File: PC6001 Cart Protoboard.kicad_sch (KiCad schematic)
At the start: 20 parts, among them J1 PC-6001 edge connector, SW1 PicoReset, SW2 EspReset, SW3 Button A, U2 ESP32-DevKitC, U3 74LS32, U4 microSD-Breakout, U5 74LS08, U6 SN74LVC245AN, U7 SN74LVC245AN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

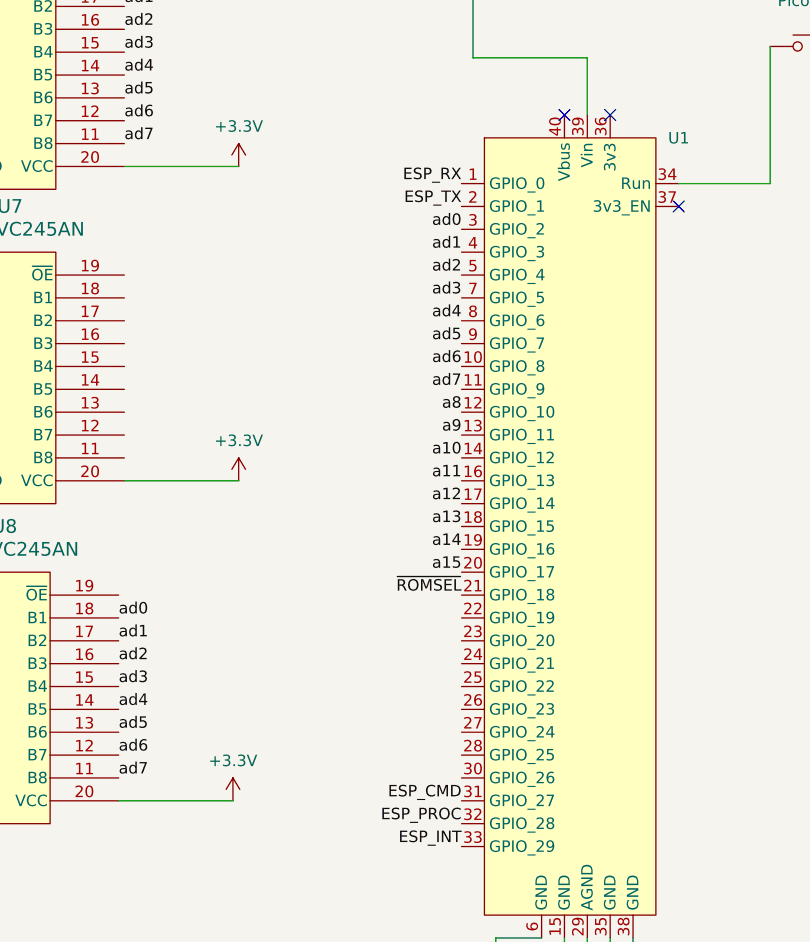
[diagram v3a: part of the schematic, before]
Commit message: Wire in ramsel and wr so now we can be sram
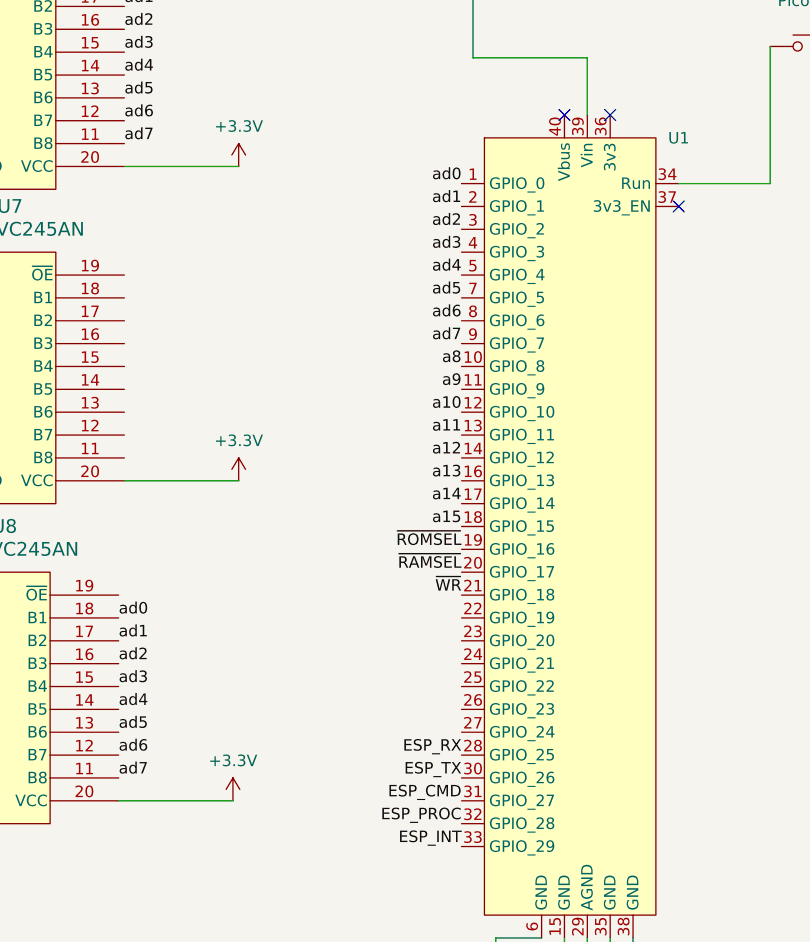
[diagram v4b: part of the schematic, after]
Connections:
- net ESP_RX: now also U1.28 (GPIO_25); no longer U1.1 (GPIO_0)
- net ESP_TX: now also U1.30 (GPIO_26); no longer U1.2 (GPIO_1)
- net a10: now also U1.12 (GPIO_10); no longer U1.14 (GPIO_12)
- net a11: now also U1.13 (GPIO_11); no longer U1.16 (GPIO_13)
- net a12: now also U1.14 (GPIO_12); no longer U1.17 (GPIO_14)
- net a13: now also U1.16 (GPIO_13); no longer U1.18 (GPIO_15)
- net a14: now also U1.17 (GPIO_14); no longer U1.19 (GPIO_16)
- net a15: now also U1.18 (GPIO_15); no longer U1.20 (GPIO_17)
- net a8: now also U1.10 (GPIO_8); no longer U1.12 (GPIO_10)
- net a9: now also U1.11 (GPIO_9); no longer U1.13 (GPIO_11)
- net ad0: now also U1.1 (GPIO_0); no longer U1.3 (GPIO_2)
- net ad1: now also U1.2 (GPIO_1); no longer U1.4 (GPIO_3)
- net ad2: now also U1.3 (GPIO_2); no longer U1.5 (GPIO_4)
- net ad3: now also U1.4 (GPIO_3); no longer U1.7 (GPIO_5)
- net ad4: now also U1.5 (GPIO_4); no longer U1.8 (GPIO_6)
- net ad5: now also U1.7 (GPIO_5); no longer U1.9 (GPIO_7)
- net ad6: now also U1.8 (GPIO_6); no longer U1.10 (GPIO_8)
- net ad7: now also U1.9 (GPIO_7); no longer U1.11 (GPIO_9)
- net ~{RAMSEL}: now also U1.20 (GPIO_17)
- net ~{ROMSEL}: now also U1.19 (GPIO_16); no longer U1.21 (GPIO_18)
- net ~{WR}: now also U1.21 (GPIO_18)
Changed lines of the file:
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@@
 	)
 	(label "a12"
-		(at 172.085 96.52 180)
+		(at 172.085 91.44 180)
 		(fields_autoplaced yes)
 		(effects
@@
 	)
 	(label "ad3"
-		(at 172.085 73.66 180)
+		(at 172.085 68.58 180)
 		(fields_autoplaced yes)
 		(effects
@@
 	)
 	(label "a11"
-		(at 172.085 93.98 180)
+		(at 172.085 88.9 180)
 		(fields_autoplaced yes)
 		(effects
@@
 	)
 	(label "a10"
-		(at 172.085 91.44 180)
+		(at 172.085 86.36 180)
 		(fields_autoplaced yes)
 		(effects
@@
 	)
 	(label "~{ROMSEL}"
-		(at 172.085 106.68 180)
+		(at 172.085 101.6 180)
 		(fields_autoplaced yes)
 		(effects
@@
 	)
 	(label "a15"
-		(at 172.085 104.14 180)
+		(at 172.085 99.06 180)
 		(fields_autoplaced yes)
 		(effects
@@
 	)
 	(label "ESP_RX"
-		(at 172.085 60.96 180)
+		(at 172.085 124.46 180)
 		(fields_autoplaced yes)
 		(effects
@@
 	)
 	(label "ESP_TX"
-		(at 172.085 63.5 180)
+		(at 172.085 127 180)
 		(fields_autoplaced yes)
 		(effects
@@
 	)
 	(label "ad4"
-		(at 172.085 76.2 180)
+		(at 172.085 71.12 180)
 		(fields_autoplaced yes)
 		(effects
@@
 	)
 	(label "a13"
-		(at 172.085 99.06 180)
+		(at 172.085 93.98 180)
 		(fields_autoplaced yes)
 		(effects
@@
 	)
 	(label "a14"
-		(at 172.085 101.6 180)
+		(at 172.085 96.52 180)
 		(fields_autoplaced yes)
 		(effects
@@
 	)
 	(label "ad5"
-		(at 172.085 78.74 180)
+		(at 172.085 73.66 180)
 		(fields_autoplaced yes)
 		(effects
@@
 		)
 	)
+	(label "~{RAMSEL}"
+		(at 172.085 104.14 180)
+		(fields_autoplaced yes)
+		(effects
+			(font
+				(size 1.27 1.27)
+			)
+			(justify right bottom)
+		)
+	)
 	(label "ad0"
-		(at 172.085 66.04 180)
+		(at 172.085 60.96 180)
 		(fields_autoplaced yes)
 		(effects
@@
 		)
 	)
+	(label "~{WR}"
+		(at 172.085 106.68 180)
+		(fields_autoplaced yes)
+		(effects
+			(font
+				(size 1.27 1.27)
+			)
+			(justify right bottom)
+		)
+	)
 	(label "a10"
 		(at 64.135 101.6 0)
@@
 	)
 	(label "ad7"
-		(at 172.085 83.82 180)
+		(at 172.085 78.74 180)
 		(fields_autoplaced yes)
 		(effects
@@
 	)
 	(label "ad1"
-		(at 172.085 68.58 180)
+		(at 172.085 63.5 180)
 		(fields_autoplaced yes)
 		(effects
@@
 	)
 	(label "a9"
-		(at 172.085 88.9 180)
+		(at 172.085 83.82 180)
 		(fields_autoplaced yes)
 		(effects
@@
 	)
 	(label "ad2"
-		(at 172.085 71.12 180)
+		(at 172.085 66.04 180)
 		(fields_autoplaced yes)
 		(effects
@@
 	)
 	(label "ad6"
-		(at 172.085 81.28 180)
+		(at 172.085 76.2 180)
 		(fields_autoplaced yes)
 		(effects
@@
 	)
 	(label "a8"
-		(at 172.085 86.36 180)
-		(fields_autoplaced yes)
-		(effects
+		(at 172.085 81.28 180)
+		(fields_autoplaced yes)
+		(effects

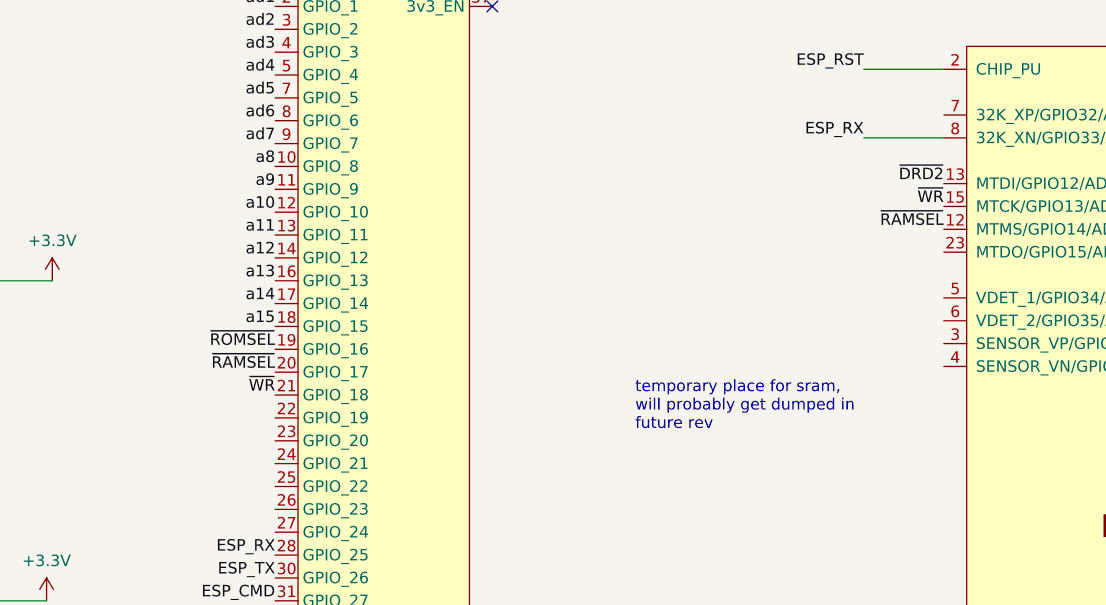
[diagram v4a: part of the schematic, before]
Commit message: Add IORQ and CS3
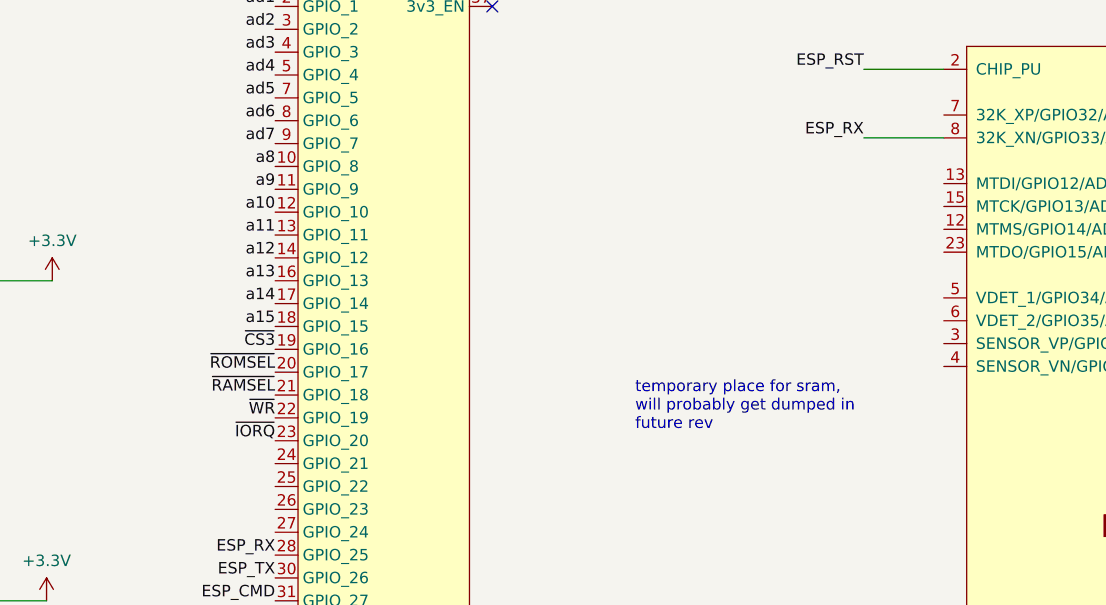
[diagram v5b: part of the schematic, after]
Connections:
- net ~{CS3}: now also U1.19 (GPIO_16)
- net ~{DRD2}: no longer U2.13 (MTDI/GPIO12/ADC2_CH5)
- net ~{RAMSEL}: now also U1.21 (GPIO_18); no longer U1.20 (GPIO_17), U2.12 (MTMS/GPIO14/ADC2_CH6)
- net ~{ROMSEL}: now also U1.20 (GPIO_17); no longer U1.19 (GPIO_16)
- net ~{WR}: now also U1.22 (GPIO_19); no longer U1.21 (GPIO_18), U2.15 (MTCK/GPIO13/ADC2_CH4)
- net ~{IORQ}: now reaches U1.23 (GPIO_20)
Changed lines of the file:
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@@
 	)
 	(label "~{ROMSEL}"
-		(at 172.085 101.6 180)
+		(at 172.085 104.14 180)
 		(fields_autoplaced yes)
 		(effects
@@
 		)
 	)
-	(label "~{DRD2}"
-		(at 246.38 83.185 180)
-		(fields_autoplaced yes)
-		(effects
-			(font
-				(size 1.27 1.27)
-			)
-			(justify right bottom)
-		)
-	)
 	(label "ad2"
 		(at 134.62 43.815 0)
@@
 		)
 	)
-	(label "~{WR}"
-		(at 246.38 85.725 180)
-		(fields_autoplaced yes)
-		(effects
-			(font
-				(size 1.27 1.27)
-			)
-			(justify right bottom)
-		)
-	)
-	(label "~{RAMSEL}"
-		(at 246.38 88.265 180)
-		(fields_autoplaced yes)
-		(effects
-			(font
-				(size 1.27 1.27)
-			)
-			(justify right bottom)
-		)
-	)
 	(label "d3"
 		(at 108.585 116.84 180)
@@
 	)
 	(label "~{RAMSEL}"
-		(at 172.085 104.14 180)
+		(at 172.085 106.68 180)
 		(fields_autoplaced yes)
 		(effects
@@
 		)
 	)
+	(label "~{CS3}"
+		(at 172.085 101.6 180)
+		(fields_autoplaced yes)
+		(effects
+			(font
+				(size 1.27 1.27)
+			)
+			(justify right bottom)
+		)
+	)
 	(label "d5"
 		(at 108.585 121.92 180)
@@
 	)
 	(label "~{WR}"
-		(at 172.085 106.68 180)
+		(at 172.085 109.22 180)
 		(fields_autoplaced yes)
 		(effects
@@
 		(fields_autoplaced yes)
 		(effects
+			(font
+				(size 1.27 1.27)
+			)
+			(justify right bottom)
+		)
+	)
+	(label "~{IORQ}"
+		(at 172.085 111.76 180)
+		(fields_autoplaced yes)
+		(effects

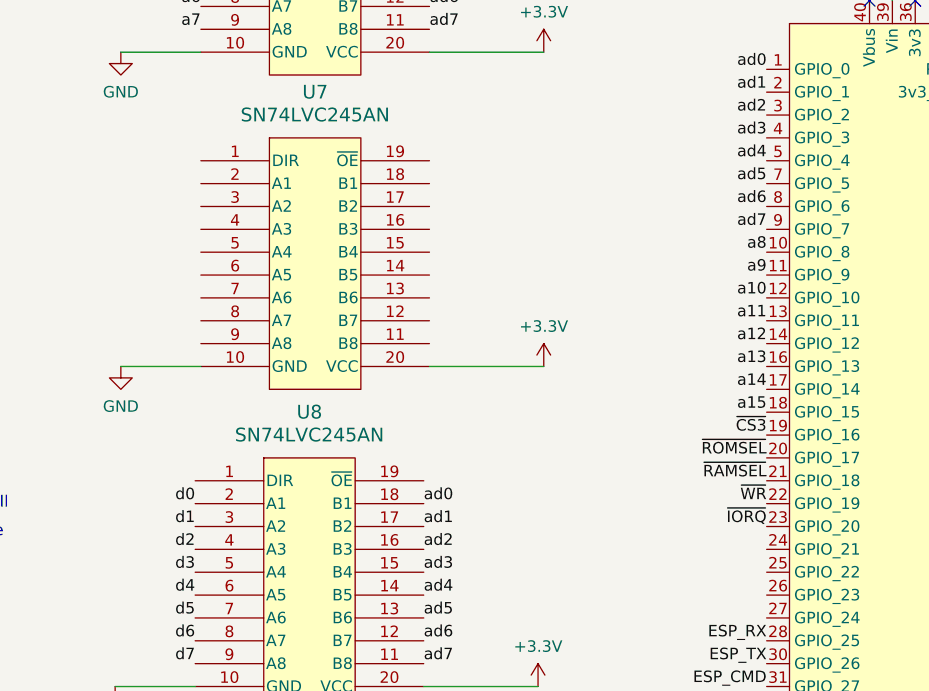
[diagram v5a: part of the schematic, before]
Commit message: Move high address lines to 245
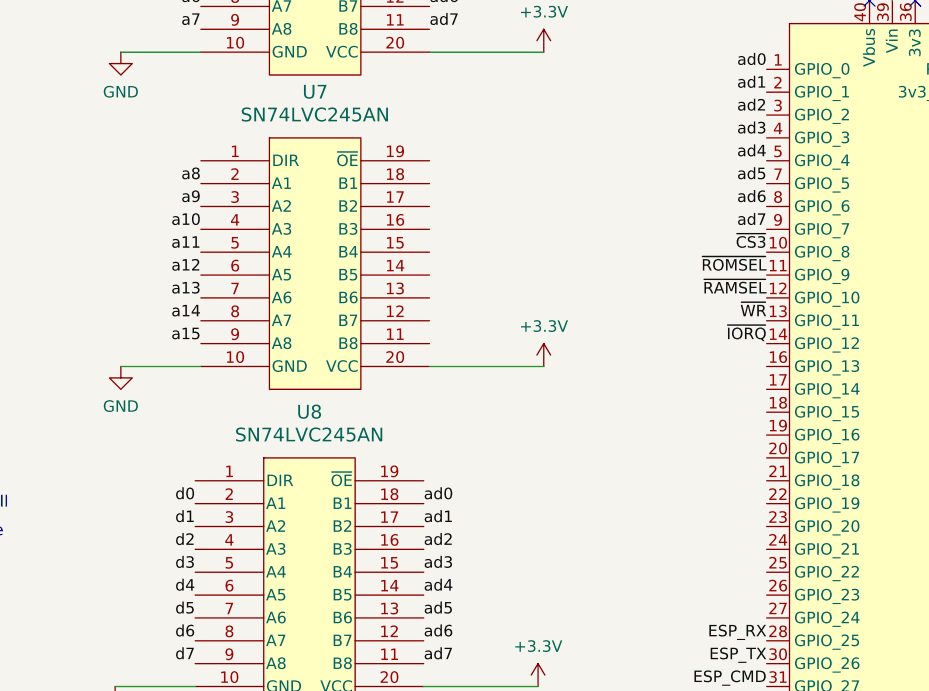
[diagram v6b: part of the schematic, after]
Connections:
- net a10: now also U7.4 (A3); no longer U1.12 (GPIO_10)
- net a11: now also U7.5 (A4); no longer U1.13 (GPIO_11)
- net a12: now also U7.6 (A5); no longer U1.14 (GPIO_12)
- net a13: now also U7.7 (A6); no longer U1.16 (GPIO_13)
- net a14: now also U7.8 (A7); no longer U1.17 (GPIO_14)
- net a15: now also U7.9 (A8); no longer U1.18 (GPIO_15)
- net a8: now also U7.2 (A1); no longer U1.10 (GPIO_8)
- net a9: now also U7.3 (A2); no longer U1.11 (GPIO_9)
- net ~{CS3}: now also U1.10 (GPIO_8); no longer U1.19 (GPIO_16)
- net ~{IORQ}: now also U1.14 (GPIO_12); no longer U1.23 (GPIO_20)
- net ~{RAMSEL}: now also U1.12 (GPIO_10); no longer U1.21 (GPIO_18)
- net ~{ROMSEL}: now also U1.11 (GPIO_9); no longer U1.20 (GPIO_17)
- net ~{WR}: now also U1.13 (GPIO_11); no longer U1.22 (GPIO_19)
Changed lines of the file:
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@@
 	)
 	(label "a12"
-		(at 172.085 91.44 180)
+		(at 109.22 83.82 180)
 		(fields_autoplaced yes)
 		(effects
@@
 	)
 	(label "a11"
-		(at 172.085 88.9 180)
+		(at 109.22 81.28 180)
 		(fields_autoplaced yes)
 		(effects
@@
 	)
 	(label "a10"
-		(at 172.085 86.36 180)
+		(at 109.22 78.74 180)
 		(fields_autoplaced yes)
 		(effects
@@
 	)
 	(label "~{ROMSEL}"
-		(at 172.085 104.14 180)
+		(at 172.085 83.82 180)
 		(fields_autoplaced yes)
 		(effects
@@
 	)
 	(label "a15"
-		(at 172.085 99.06 180)
+		(at 109.22 91.44 180)
 		(fields_autoplaced yes)
 		(effects
@@
 	)
 	(label "a13"
-		(at 172.085 93.98 180)
+		(at 109.22 86.36 180)
 		(fields_autoplaced yes)
 		(effects
@@
 	)
 	(label "a14"
-		(at 172.085 96.52 180)
+		(at 109.22 88.9 180)
 		(fields_autoplaced yes)
 		(effects
@@
 	)
 	(label "~{RAMSEL}"
-		(at 172.085 106.68 180)
+		(at 172.085 86.36 180)
 		(fields_autoplaced yes)
 		(effects
@@
 	)
 	(label "~{CS3}"
-		(at 172.085 101.6 180)
+		(at 172.085 81.28 180)
 		(fields_autoplaced yes)
 		(effects
@@
 	)
 	(label "~{WR}"
-		(at 172.085 109.22 180)
+		(at 172.085 88.9 180)
 		(fields_autoplaced yes)
 		(effects
@@
 	)
 	(label "~{IORQ}"
-		(at 172.085 111.76 180)
+		(at 172.085 91.44 180)
 		(fields_autoplaced yes)
 		(effects
@@
 	)
 	(label "a9"
-		(at 172.085 83.82 180)
+		(at 109.22 76.2 180)
 		(fields_autoplaced yes)
 		(effects
@@
 	)
 	(label "a8"
-		(at 172.085 81.28 180)
-		(fields_autoplaced yes)
-		(effects
+		(at 109.22 73.66 180)
+		(fields_autoplaced yes)
+		(effects

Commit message: Make things make more sense
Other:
- note added: "TODO: Figure out how to do direction and OE"
- note removed: "temporary place for sram, will probably get dumped in future rev"
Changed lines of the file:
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@@
+		)
+	)
+	(text "TODO: Figure out how to do direction and OE"
+		(exclude_from_sim no)
+		(at 219.71 91.44 0)
+		(effects
+			(font
+				(size 1.27 1.27)
+			)
 		)
 	)
@@
 		)
 	)
-	(text "temporary place for sram,\nwill probably get dumped in\nfuture rev"
-		(exclude_from_sim no)
-		(at 212.09 107.95 0)
-		(effects
-			(font
-				(size 1.27 1.27)
-			)
-			(justify left)
-		)
-	)

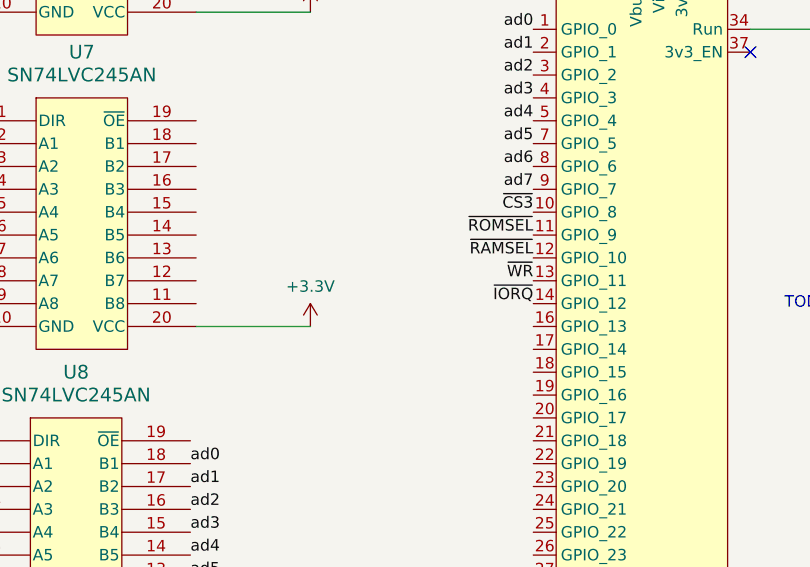
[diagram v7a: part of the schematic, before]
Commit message: RAM needs WE pin for some reason
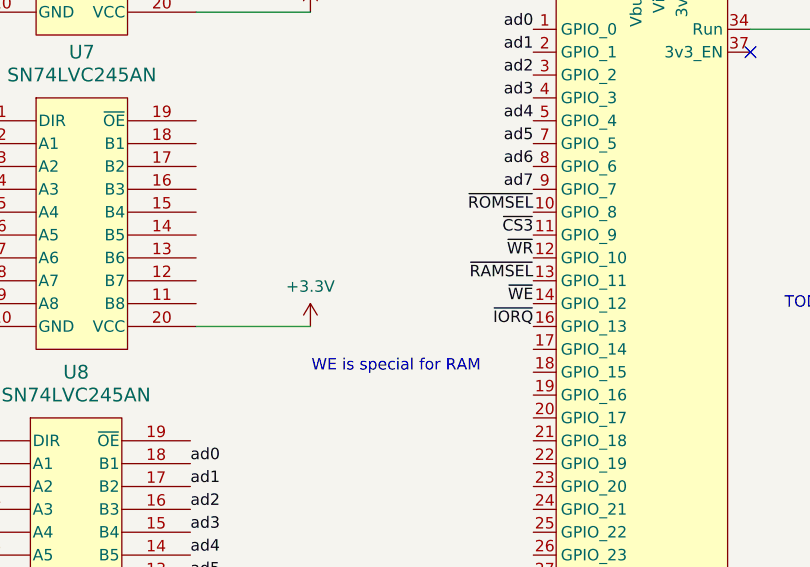
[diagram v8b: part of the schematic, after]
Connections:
- net ~{CS3}: now also U1.11 (GPIO_9); no longer U1.10 (GPIO_8)
- net ~{IORQ}: now also U1.16 (GPIO_13); no longer U1.14 (GPIO_12)
- net ~{RAMSEL}: now also U1.13 (GPIO_11); no longer U1.12 (GPIO_10)
- net ~{ROMSEL}: now also U1.10 (GPIO_8); no longer U1.11 (GPIO_9)
- net ~{WE}: now also U1.14 (GPIO_12)
- net ~{WR}: now also U1.12 (GPIO_10); no longer U1.13 (GPIO_11)
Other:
- note added: "WE is special for RAM"
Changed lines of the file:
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@@
+		)
+	)
+	(text "WE is special for RAM"
+		(exclude_from_sim no)
+		(at 156.845 98.425 0)
+		(effects
+			(font
+				(size 1.27 1.27)
+			)
 		)
 	)
@@
 	)
 	(label "~{ROMSEL}"
-		(at 172.085 83.82 180)
+		(at 172.085 81.28 180)
 		(fields_autoplaced yes)
 		(effects
@@
 	)
 	(label "~{RAMSEL}"
-		(at 172.085 86.36 180)
+		(at 172.085 88.9 180)
 		(fields_autoplaced yes)
 		(effects
@@
 	)
 	(label "~{CS3}"
-		(at 172.085 81.28 180)
+		(at 172.085 83.82 180)
 		(fields_autoplaced yes)
 		(effects
@@
 	)
 	(label "~{WR}"
-		(at 172.085 88.9 180)
+		(at 172.085 86.36 180)
 		(fields_autoplaced yes)
 		(effects
@@
 	)
 	(label "~{IORQ}"
-		(at 172.085 91.44 180)
+		(at 172.085 93.98 180)
 		(fields_autoplaced yes)
 		(effects
@@
 		)
 	)
+	(label "~{WE}"
+		(at 172.085 91.44 180)
+		(fields_autoplaced yes)
+		(effects
+			(font
+				(size 1.27 1.27)
+			)
+			(justify right bottom)
+		)
+	)
